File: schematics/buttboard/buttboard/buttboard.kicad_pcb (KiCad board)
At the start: 2 copper layers, 84 x 65 mm, 20 parts, among them J1 Conn_01x05, J5 527461671, SW1 N, SW2 S, SW3 E, SW4 W, SW5 A, SW6 B, SW7 C, SW8 D

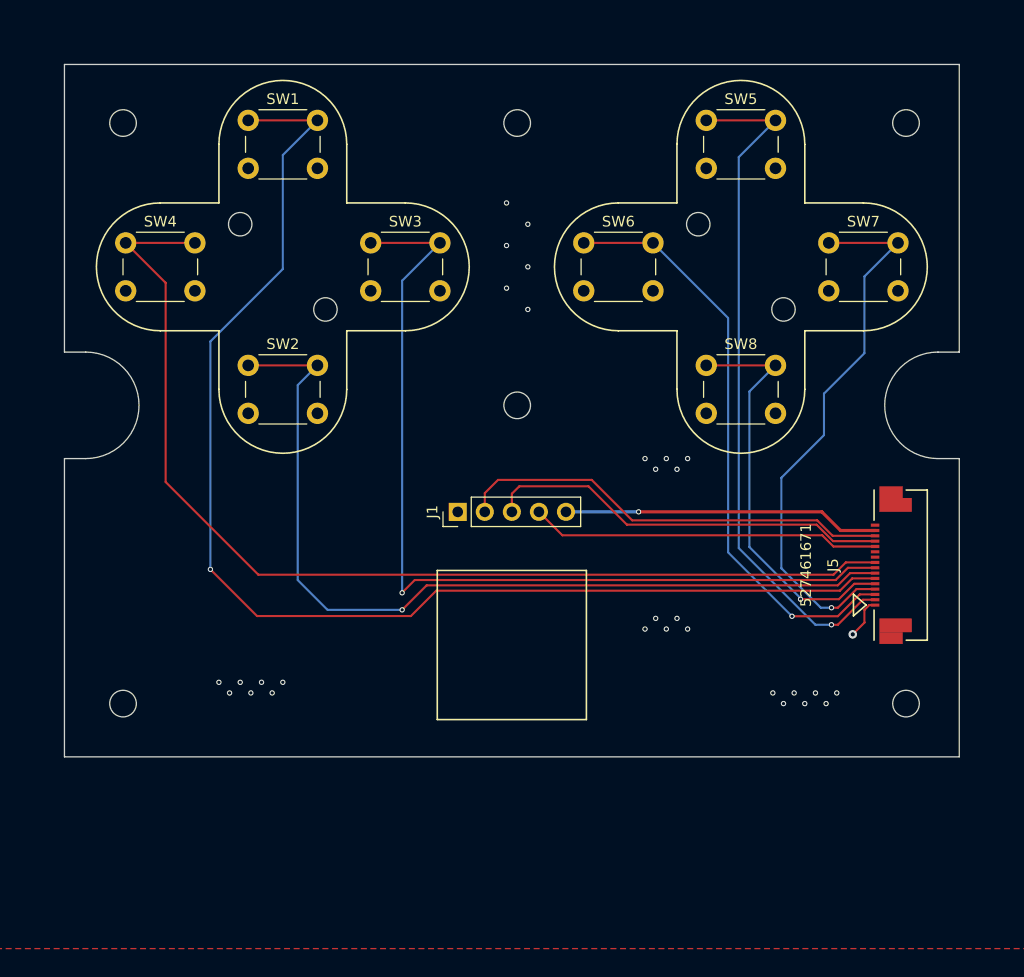
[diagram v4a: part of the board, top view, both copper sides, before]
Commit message: Added control buttons to buttboard; adjusted cutout.
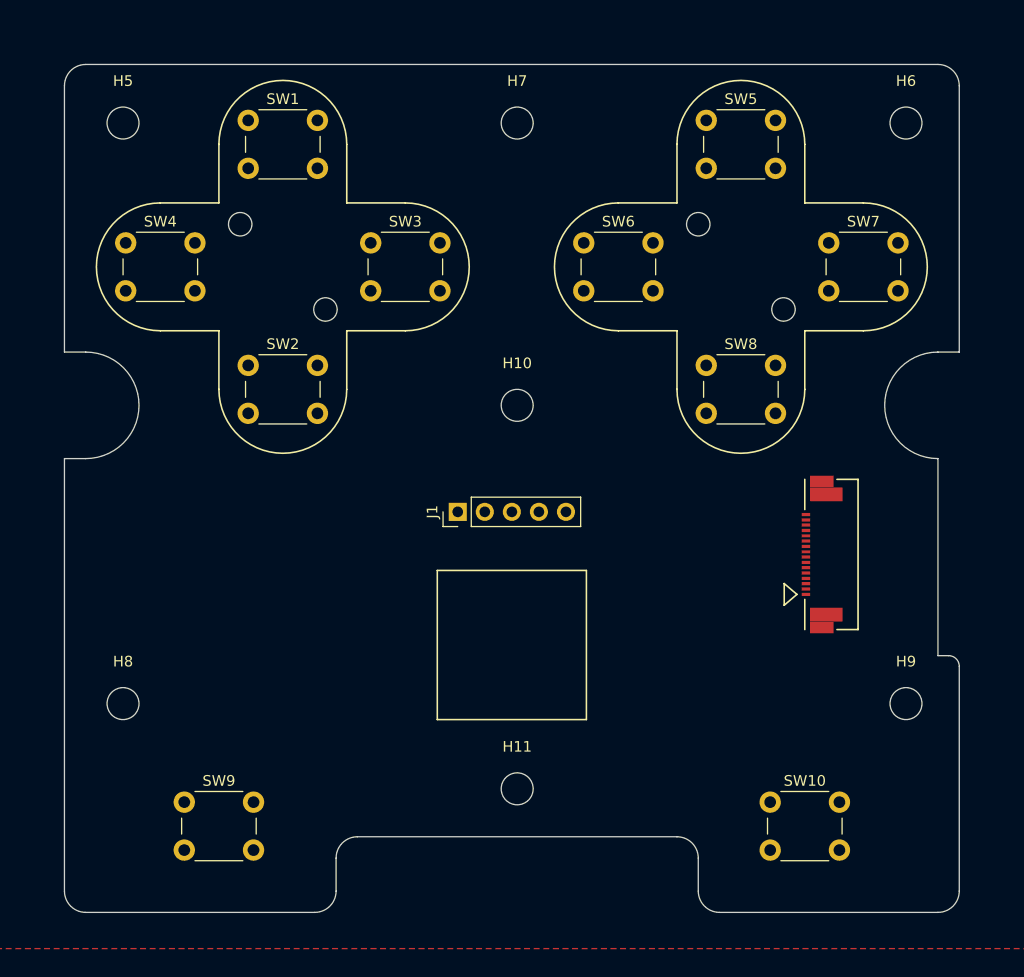
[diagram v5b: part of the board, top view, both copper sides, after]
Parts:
- added H11: MountingHole, MountingHole:MountingHole_3mm, F.Cu at (153.0, 125.0)
- added SW10: B, Button_Switch_THT:SW_PUSH_6mm_H7.3mm, F.Cu at (176.8, 126.2)
- added SW9: A, Button_Switch_THT:SW_PUSH_6mm_H7.3mm, F.Cu at (121.8, 126.2)
- H10, H5, H6, H7, H8, H9: footprint MountingHole:MountingHole_2.5mm -> MountingHole:MountingHole_3mm
- moved J5 6.58 mm to (182.5, 103.0)
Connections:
- J5 pad 10: unconnected-(J5-Pad10) -> BTN_SELECT
- J5 pad 11: unconnected-(J5-Pad11) -> BTN_CANCEL
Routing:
- net BTN_DPAD_N: track 118.5 -> 0.00 mm, vias 1 -> 0
- net BTN_DPAD_W: track 101.2 -> 0.00 mm
- net BTN_DPAD_E: track 86.2 -> 0.00 mm, vias 1 -> 0
- net BTN_DPAD_S: track 84.2 -> 0.00 mm, vias 1 -> 0
- net BTN_A: track 64.8 -> 0.00 mm, vias 1 -> 0
- net BTN_B: track 55.6 -> 0.00 mm, vias 1 -> 0
- net BTN_C: track 52.6 -> 0.00 mm, vias 1 -> 0
- net TRACKBALL_INTERRUPT: track 41.1 -> 0.00 mm
- net BTN_D: track 39.1 -> 0.00 mm, vias 1 -> 0
- net I2C_SCL: track 38.2 -> 0.00 mm
- net I2C_SDA: track 32.9 -> 0.00 mm
- net 3V3: track 29.7 -> 0.00 mm, vias 1 -> 0
- net GND: track 3.94 -> 0.00 mm, vias 31 -> 0
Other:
- board size 84 x 65 mm -> 84 x 79.6 mm

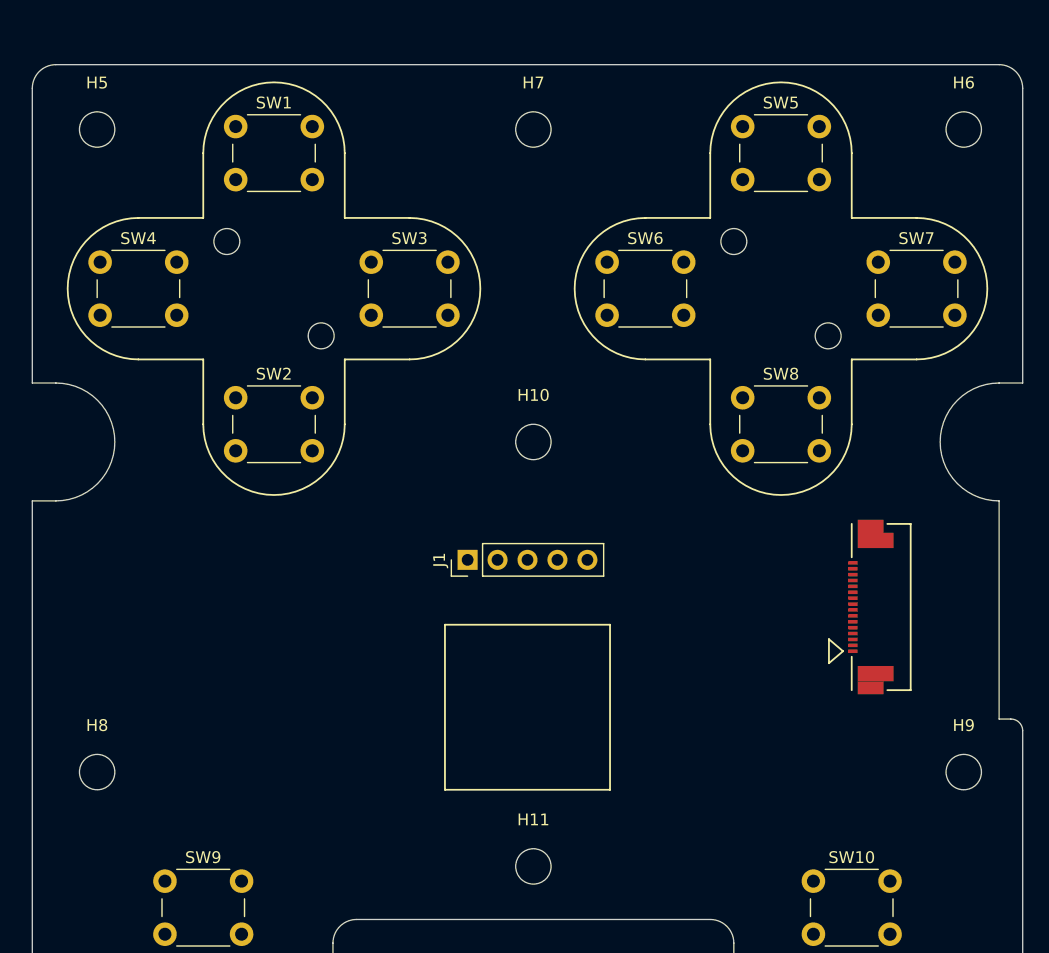
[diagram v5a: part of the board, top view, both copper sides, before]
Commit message: Button board ordered from JLCPCB.
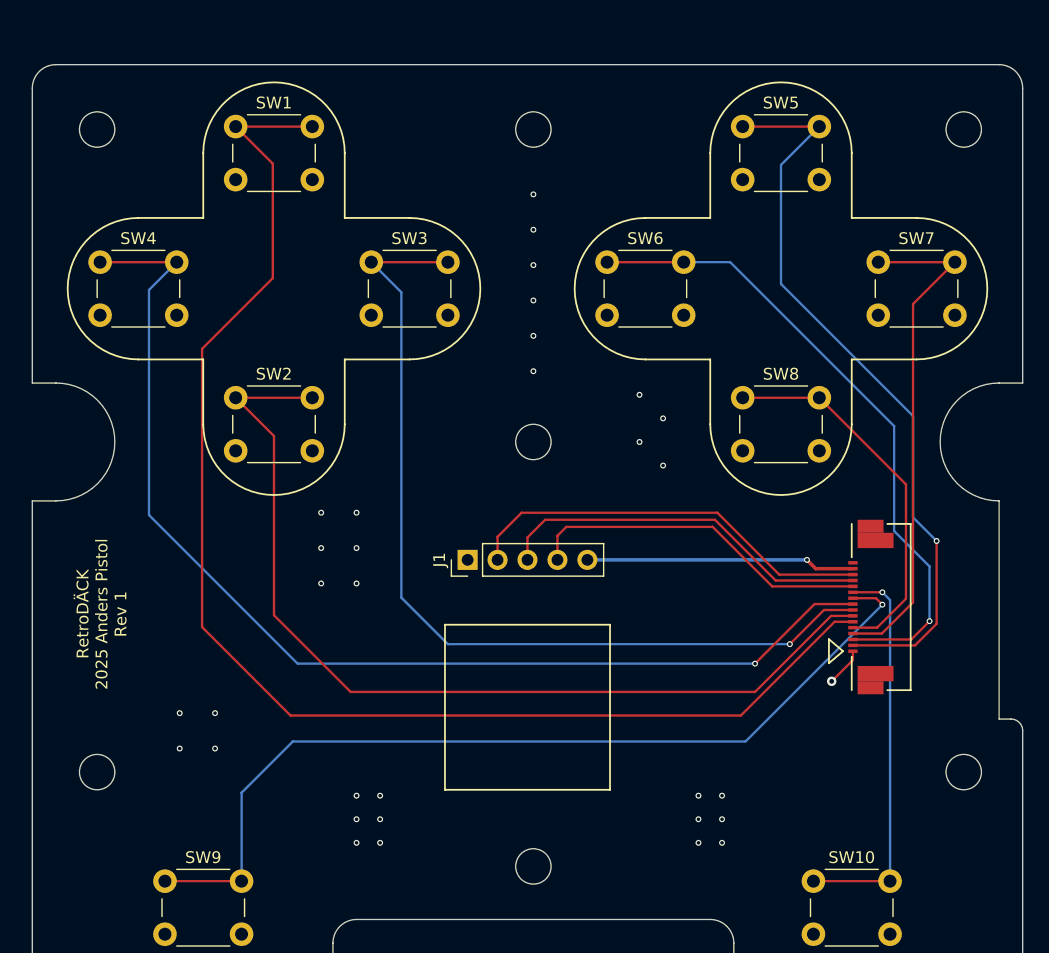
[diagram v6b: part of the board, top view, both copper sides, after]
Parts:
- removed H1, H2, H3, H4: MountingHole, MountingHole:MountingHole_2.2mm_M2
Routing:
- net BTN_DPAD_N: track 0.00 -> 114.3 mm
- net BTN_DPAD_W: track 0.00 -> 95.9 mm, vias 0 -> 1
- net BTN_DPAD_S: track 0.00 -> 80.8 mm
- net BTN_SELECT: track 0.00 -> 77.7 mm, vias 0 -> 1
- net BTN_DPAD_E: track 0.00 -> 77.1 mm, vias 0 -> 1
- net BTN_A: track 0.00 -> 63.3 mm, vias 0 -> 1
- net BTN_B: track 0.00 -> 55.0 mm, vias 0 -> 1
- net BTN_C: track 0.00 -> 43.0 mm
- net TRACKBALL_INTERRUPT: track 0.00 -> 35.1 mm
- net BTN_CANCEL: track 0.00 -> 33.8 mm, vias 0 -> 1
- net I2C_SCL: track 0.00 -> 32.3 mm
- net BTN_D: track 0.00 -> 32.1 mm
- net I2C_SDA: track 0.00 -> 29.5 mm
- net 3V3: track 0.00 -> 22.8 mm, vias 0 -> 1
- net GND: track 0.00 -> 3.30 mm, vias 0 -> 33
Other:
- board text added: "RetroDÄCK 2025 Anders Pistol Rev 1"
